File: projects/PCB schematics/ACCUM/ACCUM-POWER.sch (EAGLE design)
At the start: 8 parts, among them J1 2P(90DEG)_1-770966-0, J2 2P(90DEG)_1-770966-0, J3 2P(90DEG)_1-770966-0

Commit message: ACCUM - Rev A.
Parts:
- renumbered C11 to C3, C14 to C1, C15 to C2
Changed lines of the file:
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@@
 <part name="PS1" library="M57184N-715B" deviceset="M57184N-715B" device=""/>
 <part name="L1" library="rcl" library_urn="urn:adsk.eagle:library:334" deviceset="L-US" device="L2012C" package3d_urn="urn:adsk.eagle:package:23475/2" value="1mH"/>
-<part name="C11" library="EEU-FS1H221L" deviceset="EEU-FS1H221L" device=""/>
+<part name="C3" library="EEU-FS1H221L" deviceset="EEU-FS1H221L" device=""/>
 <part name="SUPPLY16" library="supply2" library_urn="urn:adsk.eagle:library:372" deviceset="GND" device="" value="HV-"/>
 <part name="SUPPLY17" library="supply2" library_urn="urn:adsk.eagle:library:372" deviceset="GND" device="" value="HV-"/>
-<part name="C14" library="EKXF451ELL100MJ20S" deviceset="EKXF451ELL100MJ20S" device=""/>
-<part name="C15" library="EKXF451ELL100MJ20S" deviceset="EKXF451ELL100MJ20S" device=""/>
+<part name="C1" library="EKXF451ELL100MJ20S" deviceset="EKXF451ELL100MJ20S" device=""/>
+<part name="C2" library="EKXF451ELL100MJ20S" deviceset="EKXF451ELL100MJ20S" device=""/>
 <part name="J1" library="con-MATE-N-LOK" deviceset="2P(90DEG)_1-770966-0" device=""/>
 <part name="J2" library="con-MATE-N-LOK" deviceset="2P(90DEG)_1-770966-0" device=""/>
@@
 <attribute name="VALUE" x="57.15" y="38.1" size="1.778" layer="96" rot="R90"/>
 </instance>
-<instance part="C11" gate="G$1" x="66.04" y="45.72" smashed="yes" rot="R270">
+<instance part="C3" gate="G$1" x="66.04" y="45.72" smashed="yes" rot="R270">
 <attribute name="NAME" x="69.85" y="44.45" size="1.778" layer="95" rot="MR180" align="center-left"/>
 <attribute name="VALUE" x="69.85" y="39.37" size="1.778" layer="96" align="center-left"/>
@@
 <attribute name="VALUE" x="41.275" y="17.145" size="1.778" layer="96"/>
 </instance>
-<instance part="C14" gate="G$1" x="43.18" y="55.88" smashed="yes" rot="R270">
+<instance part="C1" gate="G$1" x="43.18" y="55.88" smashed="yes" rot="R270">
 <attribute name="NAME" x="39.37" y="52.07" size="1.778" layer="95" rot="R180" align="center-left"/>
 <attribute name="VALUE" x="11.43" y="46.99" size="1.778" layer="96" align="center-left"/>
 </instance>
-<instance part="C15" gate="G$1" x="43.18" y="40.64" smashed="yes" rot="R270">
+<instance part="C2" gate="G$1" x="43.18" y="40.64" smashed="yes" rot="R270">
 <attribute name="NAME" x="39.37" y="36.83" size="1.778" layer="95" rot="R180" align="center-left"/>
 <attribute name="VALUE" x="11.43" y="31.75" size="1.778" layer="96" align="center-left"/>
@@
 </segment>
 <segment>
-<pinref part="C11" gate="G$1" pin="-"/>
+<pinref part="C3" gate="G$1" pin="-"/>
 <pinref part="SUPPLY16" gate="GND" pin="GND"/>
 <wire x1="66.04" y1="33.02" x2="66.04" y2="25.4" width="0.1524" layer="91"/>
@@
 <pinref part="SUPPLY17" gate="GND" pin="GND"/>
 <wire x1="43.18" y1="22.86" x2="43.18" y2="27.94" width="0.1524" layer="91"/>
-<pinref part="C15" gate="G$1" pin="-"/>
+<pinref part="C2" gate="G$1" pin="-"/>
 </segment>
 <segment>
@@
 <wire x1="83.82" y1="58.42" x2="43.18" y2="58.42" width="0.1524" layer="91"/>
 <wire x1="43.18" y1="58.42" x2="43.18" y2="55.88" width="0.1524" layer="91"/>
-<pinref part="C14" gate="G$1" pin="+"/>
+<pinref part="C1" gate="G$1" pin="+"/>
 </segment>
 <segment>
@@
 <label x="66.04" y="48.26" size="1.778" layer="95"/>
 <wire x1="83.82" y1="48.26" x2="66.04" y2="48.26" width="0.1524" layer="91"/>
-<pinref part="C11" gate="G$1" pin="+"/>
+<pinref part="C3" gate="G$1" pin="+"/>
 <wire x1="66.04" y1="45.72" x2="66.04" y2="48.26" width="0.1524" layer="91"/>
 </segment>
@@
 <segment>
 <wire x1="43.18" y1="43.18" x2="43.18" y2="40.64" width="0.1524" layer="91"/>
-<pinref part="C14" gate="G$1" pin="-"/>
-<pinref part="C15" gate="G$1" pin="+"/>
+<pinref part="C1" gate="G$1" pin="-"/>
+<pinref part="C2" gate="G$1" pin="+"/>
 </segment>
 </net>

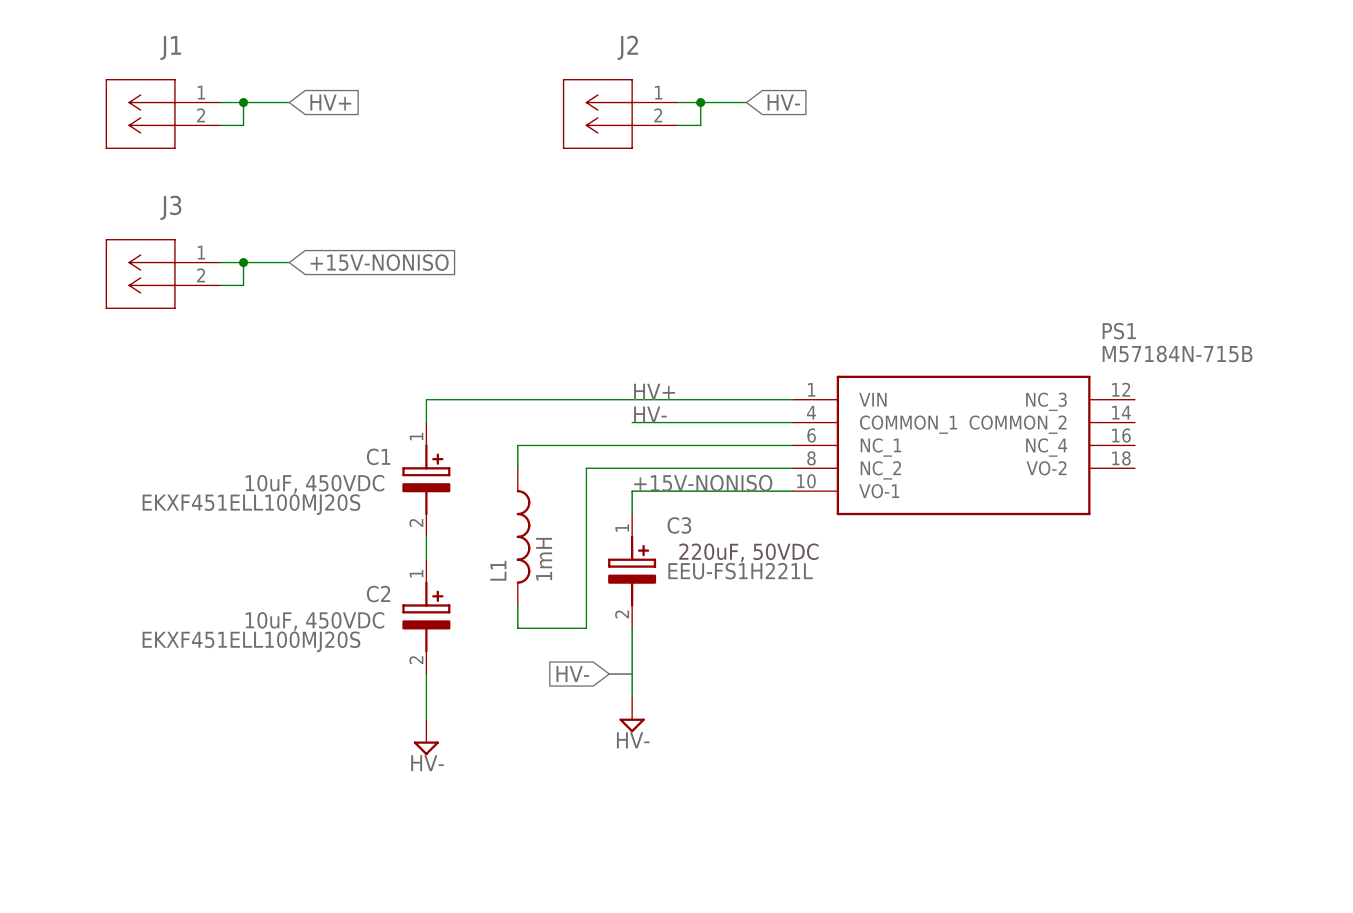
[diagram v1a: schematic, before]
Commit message: TSAL - Added in fuses.
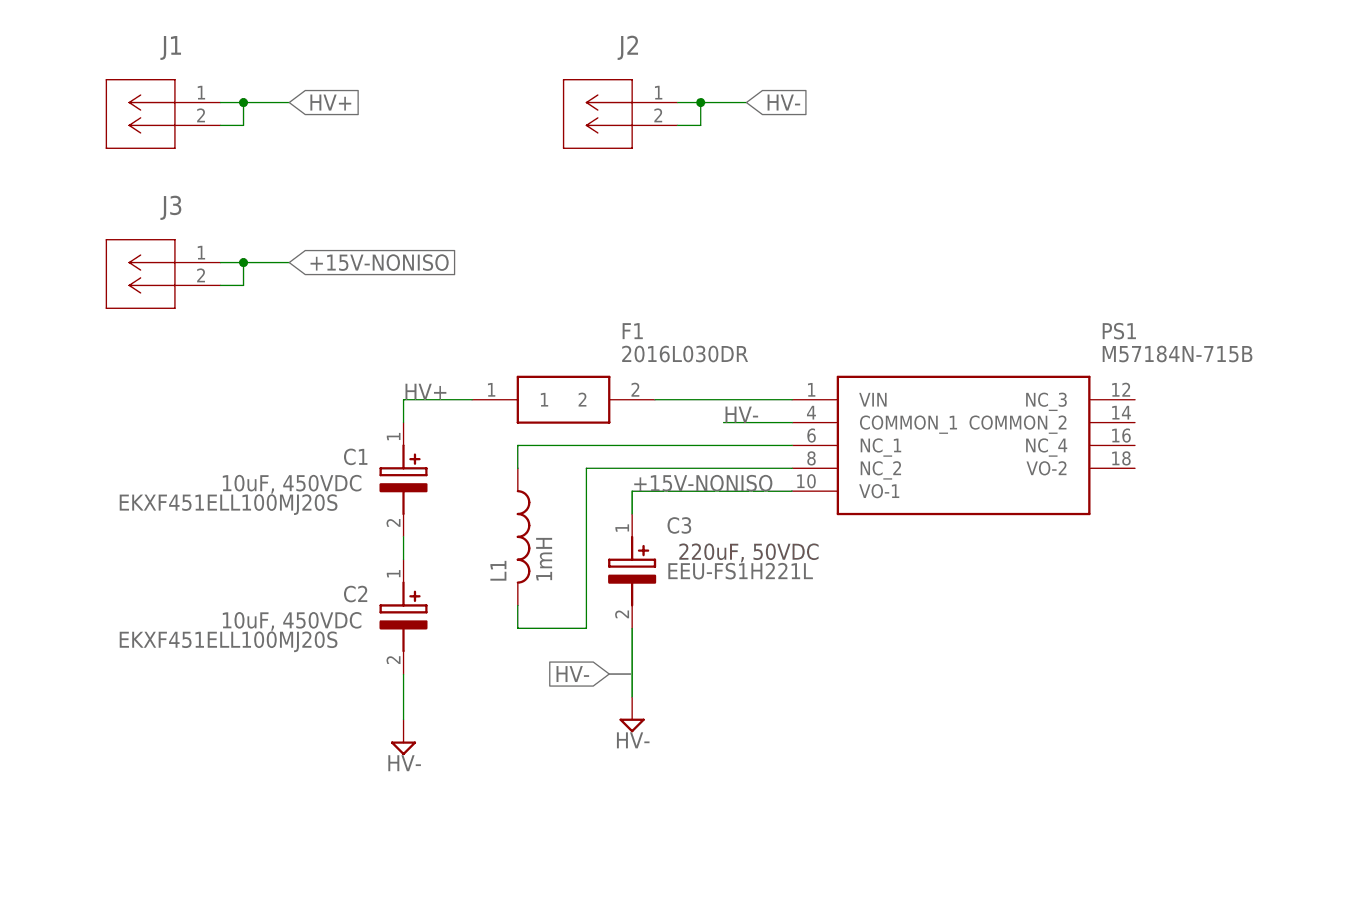
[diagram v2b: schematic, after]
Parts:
- added F1: 2016L030DR, SamacSys_Parts:2016L030DR
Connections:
- new net N$4: F1.2, PS1.VIN
- net HV+: now also F1.1; no longer PS1.VIN
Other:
- moved on the sheet: C1, C2
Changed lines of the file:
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@@
 <?xml version="1.0" encoding="utf-8"?>
 <!DOCTYPE eagle SYSTEM "eagle.dtd">
-<eagle version="9.3.2">
+<eagle version="9.4.0">
 <drawing>
 <settings>
@@
 <part name="J2" library="con-MATE-N-LOK" deviceset="2P(90DEG)_1-770966-0" device=""/>
 <part name="J3" library="con-MATE-N-LOK" deviceset="2P(90DEG)_1-770966-0" device=""/>
+<part name="F1" library="SamacSys_Parts" deviceset="2016L030DR" device=""/>
 </parts>
 <sheets>
@@
 <text x="71.12" y="40.64" size="1.778" layer="97">220uF, 50VDC</text>
 <wire x1="63.5" y1="27.94" x2="66.04" y2="27.94" width="0.1524" layer="97"/>
-<text x="22.86" y="48.26" size="1.778" layer="96">10uF, 450VDC</text>
-<text x="22.86" y="33.02" size="1.778" layer="96">10uF, 450VDC</text>
+<text x="20.32" y="48.26" size="1.778" layer="96">10uF, 450VDC</text>
+<text x="20.32" y="33.02" size="1.778" layer="96">10uF, 450VDC</text>
 </plain>
 <instances>
@@
 <attribute name="VALUE" x="64.135" y="19.685" size="1.778" layer="96"/>
 </instance>
-<instance part="SUPPLY17" gate="GND" x="43.18" y="20.32" smashed="yes">
-<attribute name="VALUE" x="41.275" y="17.145" size="1.778" layer="96"/>
-</instance>
-<instance part="C1" gate="G$1" x="43.18" y="55.88" smashed="yes" rot="R270">
-<attribute name="NAME" x="39.37" y="52.07" size="1.778" layer="95" rot="R180" align="center-left"/>
-<attribute name="VALUE" x="11.43" y="46.99" size="1.778" layer="96" align="center-left"/>
-</instance>
-<instance part="C2" gate="G$1" x="43.18" y="40.64" smashed="yes" rot="R270">
-<attribute name="NAME" x="39.37" y="36.83" size="1.778" layer="95" rot="R180" align="center-left"/>
-<attribute name="VALUE" x="11.43" y="31.75" size="1.778" layer="96" align="center-left"/>
+<instance part="SUPPLY17" gate="GND" x="40.64" y="20.32" smashed="yes">
+<attribute name="VALUE" x="38.735" y="17.145" size="1.778" layer="96"/>
+</instance>
+<instance part="C1" gate="G$1" x="40.64" y="55.88" smashed="yes" rot="R270">
+<attribute name="NAME" x="36.83" y="52.07" size="1.778" layer="95" rot="R180" align="center-left"/>
+<attribute name="VALUE" x="8.89" y="46.99" size="1.778" layer="96" align="center-left"/>
+</instance>
+<instance part="C2" gate="G$1" x="40.64" y="40.64" smashed="yes" rot="R270">
+<attribute name="NAME" x="36.83" y="36.83" size="1.778" layer="95" rot="R180" align="center-left"/>
+<attribute name="VALUE" x="8.89" y="31.75" size="1.778" layer="96" align="center-left"/>
 </instance>
 <instance part="J1" gate="A" x="20.32" y="91.44" smashed="yes" rot="MR0">
@@
 <instance part="J3" gate="A" x="20.32" y="73.66" smashed="yes" rot="MR0">
 <attribute name="NAME" x="16.1544" y="78.9686" size="2.0828" layer="95" ratio="6" rot="SMR0"/>
+</instance>
+<instance part="F1" gate="G$1" x="48.26" y="58.42" smashed="yes">
+<attribute name="NAME" x="64.77" y="66.04" size="1.778" layer="95" align="center-left"/>
+<attribute name="VALUE" x="64.77" y="63.5" size="1.778" layer="96" align="center-left"/>
 </instance>
 </instances>
@@
 <segment>
 <pinref part="PS1" gate="G$1" pin="COMMON_1"/>
-<wire x1="83.82" y1="55.88" x2="66.04" y2="55.88" width="0.1524" layer="91"/>
-<label x="66.04" y="55.88" size="1.778" layer="95"/>
+<wire x1="83.82" y1="55.88" x2="76.2" y2="55.88" width="0.1524" layer="91"/>
+<label x="76.2" y="55.88" size="1.778" layer="95"/>
 </segment>
 <segment>
@@
 <segment>
 <pinref part="SUPPLY17" gate="GND" pin="GND"/>
-<wire x1="43.18" y1="22.86" x2="43.18" y2="27.94" width="0.1524" layer="91"/>
+<wire x1="40.64" y1="22.86" x2="40.64" y2="27.94" width="0.1524" layer="91"/>
 <pinref part="C2" gate="G$1" pin="-"/>
 </segment>
@@
 <net name="HV+" class="0">
 <segment>
-<pinref part="PS1" gate="G$1" pin="VIN"/>
-<label x="66.04" y="58.42" size="1.778" layer="95"/>
-<wire x1="83.82" y1="58.42" x2="43.18" y2="58.42" width="0.1524" layer="91"/>
-<wire x1="43.18" y1="58.42" x2="43.18" y2="55.88" width="0.1524" layer="91"/>
+<label x="40.64" y="58.42" size="1.778" layer="95"/>
+<wire x1="40.64" y1="58.42" x2="40.64" y2="55.88" width="0.1524" layer="91"/>
 <pinref part="C1" gate="G$1" pin="+"/>
+<pinref part="F1" gate="G$1" pin="1"/>
+<wire x1="48.26" y1="58.42" x2="40.64" y2="58.42" width="0.1524" layer="91"/>
 </segment>
 <segment>
@@
 <net name="N$3" class="0">
 <segment>
-<wire x1="43.18" y1="43.18" x2="43.18" y2="40.64" width="0.1524" layer="91"/>
+<wire x1="40.64" y1="43.18" x2="40.64" y2="40.64" width="0.1524" layer="91"/>
 <pinref part="C1" gate="G$1" pin="-"/>
 <pinref part="C2" gate="G$1" pin="+"/>
 </segment>
 </net>
+<net name="N$4" class="0">
+<segment>
+<pinref part="F1" gate="G$1" pin="2"/>
+<pinref part="PS1" gate="G$1" pin="VIN"/>
+<wire x1="68.58" y1="58.42" x2="83.82" y2="58.42" width="0.1524" layer="91"/>
+</segment>
+</net>
